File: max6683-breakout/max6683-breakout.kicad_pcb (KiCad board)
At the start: 2 copper layers, 11 parts, among them J1 Conn_01x05, J2 Conn_01x05, U1 MAX6683

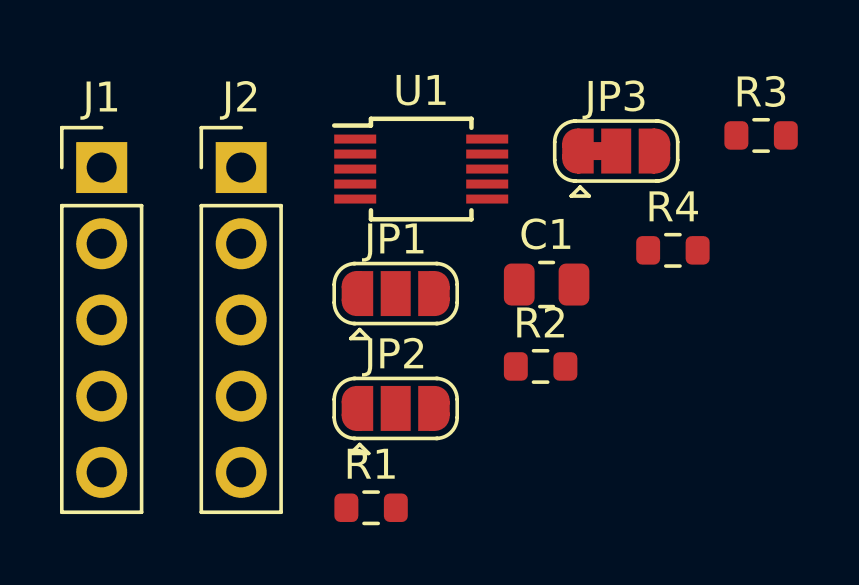
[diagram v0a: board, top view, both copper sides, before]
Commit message: Transition project to KiCad 6
Supports #44.
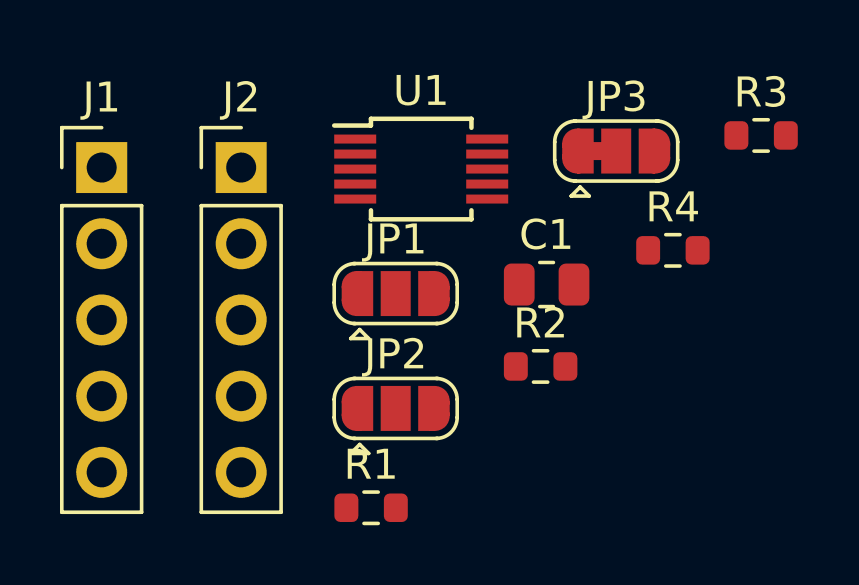
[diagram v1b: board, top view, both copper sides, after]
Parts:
- JP1: value I2C -> SolderJumper_3_Open
- JP2: value SCL -> SolderJumper_3_Open
- JP3: value SDA -> SolderJumper_3_Bridged12
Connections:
- C1 pad 1: Net-(C1-Pad1) -> unconnected-(C1-Pad1)
- C1 pad 2: Net-(C1-Pad2) -> unconnected-(C1-Pad2)
- J1 pad 1: Net-(J1-Pad1) -> unconnected-(J1-Pad1)
- J1 pad 2: Net-(J1-Pad2) -> unconnected-(J1-Pad2)
- J1 pad 3: Net-(J1-Pad3) -> unconnected-(J1-Pad3)
- J1 pad 4: Net-(J1-Pad4) -> unconnected-(J1-Pad4)
- J1 pad 5: Net-(J1-Pad5) -> unconnected-(J1-Pad5)
- J2 pad 1: Net-(J2-Pad1) -> unconnected-(J2-Pad1)
- J2 pad 2: Net-(J2-Pad2) -> unconnected-(J2-Pad2)
- J2 pad 3: Net-(J2-Pad3) -> unconnected-(J2-Pad3)
- J2 pad 4: Net-(J2-Pad4) -> unconnected-(J2-Pad4)
- J2 pad 5: Net-(J2-Pad5) -> unconnected-(J2-Pad5)
- JP1 pad 1: Net-(JP1-Pad1) -> unconnected-(JP1-Pad1)
- JP1 pad 2: Net-(JP1-Pad2) -> unconnected-(JP1-Pad2)
- JP1 pad 3: Net-(JP1-Pad3) -> unconnected-(JP1-Pad3)
- JP2 pad 1: Net-(JP2-Pad1) -> unconnected-(JP2-Pad1)
- JP2 pad 2: Net-(JP2-Pad2) -> unconnected-(JP2-Pad2)
- JP2 pad 3: Net-(JP2-Pad3) -> unconnected-(JP2-Pad3)
- JP3 pad 1: Net-(JP3-Pad1) -> unconnected-(JP3-Pad1)
- JP3 pad 2: Net-(JP3-Pad2) -> unconnected-(JP3-Pad2)
- JP3 pad 3: Net-(JP3-Pad3) -> unconnected-(JP3-Pad3)
- R1 pad 1: Net-(R1-Pad1) -> unconnected-(R1-Pad1)
- R1 pad 2: Net-(R1-Pad2) -> unconnected-(R1-Pad2)
- R2 pad 1: Net-(R2-Pad1) -> unconnected-(R2-Pad1)
- R2 pad 2: Net-(R2-Pad2) -> unconnected-(R2-Pad2)
- R3 pad 1: Net-(R3-Pad1) -> unconnected-(R3-Pad1)
- R3 pad 2: Net-(R3-Pad2) -> unconnected-(R3-Pad2)
- R4 pad 1: Net-(R4-Pad1) -> unconnected-(R4-Pad1)
- R4 pad 2: Net-(R4-Pad2) -> unconnected-(R4-Pad2)
- U1 pad 1: Net-(U1-Pad1) -> unconnected-(U1-Pad1)
- U1 pad 10: Net-(U1-Pad10) -> unconnected-(U1-Pad10)
- U1 pad 2: Net-(U1-Pad2) -> unconnected-(U1-Pad2)
- U1 pad 3: Net-(U1-Pad3) -> unconnected-(U1-Pad3)
- U1 pad 4: Net-(U1-Pad4) -> unconnected-(U1-Pad4)
- U1 pad 5: Net-(U1-Pad5) -> unconnected-(U1-Pad5)
- U1 pad 6: Net-(U1-Pad6) -> unconnected-(U1-Pad6)
- U1 pad 7: Net-(U1-Pad7) -> unconnected-(U1-Pad7)
- U1 pad 8: Net-(U1-Pad8) -> unconnected-(U1-Pad8)
- U1 pad 9: Net-(U1-Pad9) -> unconnected-(U1-Pad9)
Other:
- net class Default removed

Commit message: Connect schematic nets
Supports #44.
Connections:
- C1 pad 1: unconnected-(C1-Pad1) -> +3V3
- C1 pad 2: unconnected-(C1-Pad2) -> GND
- J1 pad 1: unconnected-(J1-Pad1) -> Net-(U1-Pad1)
- J1 pad 2: unconnected-(J1-Pad2) -> Net-(U1-Pad2)
- J1 pad 3: unconnected-(J1-Pad3) -> Net-(U1-Pad3)
- J1 pad 5: unconnected-(J1-Pad5) -> GND
- J2 pad 1: unconnected-(J2-Pad1) -> Net-(U1-Pad6)
- J2 pad 2: unconnected-(J2-Pad2) -> ADD
- J2 pad 3: unconnected-(J2-Pad3) -> SDA
- J2 pad 4: unconnected-(J2-Pad4) -> SCL
- J2 pad 5: unconnected-(J2-Pad5) -> +3V3
- JP1 pad 1: unconnected-(JP1-Pad1) -> Net-(R2-Pad1)
- JP1 pad 2: unconnected-(JP1-Pad2) -> +3V3
- JP1 pad 3: unconnected-(JP1-Pad3) -> Net-(R1-Pad1)
- JP2 pad 1: unconnected-(JP2-Pad1) -> Net-(JP2-Pad1)
- JP2 pad 2: unconnected-(JP2-Pad2) -> ADD
- JP2 pad 3: unconnected-(JP2-Pad3) -> SCL
- JP3 pad 1: unconnected-(JP3-Pad1) -> SDA
- JP3 pad 2: unconnected-(JP3-Pad2) -> ADD
- JP3 pad 3: unconnected-(JP3-Pad3) -> GND
- R1 pad 1: unconnected-(R1-Pad1) -> Net-(R1-Pad1)
- R1 pad 2: unconnected-(R1-Pad2) -> SCL
- R2 pad 1: unconnected-(R2-Pad1) -> Net-(R2-Pad1)
- R2 pad 2: unconnected-(R2-Pad2) -> SDA
- R3 pad 1: unconnected-(R3-Pad1) -> +3V3
- R4 pad 1: unconnected-(R4-Pad1) -> +3V3
- R4 pad 2: unconnected-(R4-Pad2) -> Net-(JP2-Pad1)
- U1 pad 1: unconnected-(U1-Pad1) -> Net-(U1-Pad1)
- U1 pad 10: unconnected-(U1-Pad10) -> +3V3
- U1 pad 2: unconnected-(U1-Pad2) -> Net-(U1-Pad2)
- U1 pad 3: unconnected-(U1-Pad3) -> Net-(U1-Pad3)
- U1 pad 5: unconnected-(U1-Pad5) -> GND
- U1 pad 6: unconnected-(U1-Pad6) -> Net-(U1-Pad6)
- U1 pad 7: unconnected-(U1-Pad7) -> ADD
- U1 pad 8: unconnected-(U1-Pad8) -> SDA
- U1 pad 9: unconnected-(U1-Pad9) -> SCL
